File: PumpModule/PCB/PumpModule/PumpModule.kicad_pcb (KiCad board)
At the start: 2 copper layers, 8 parts, among them J5 Conn_01x04, J6 Conn_01x04, J7 Conn_01x03

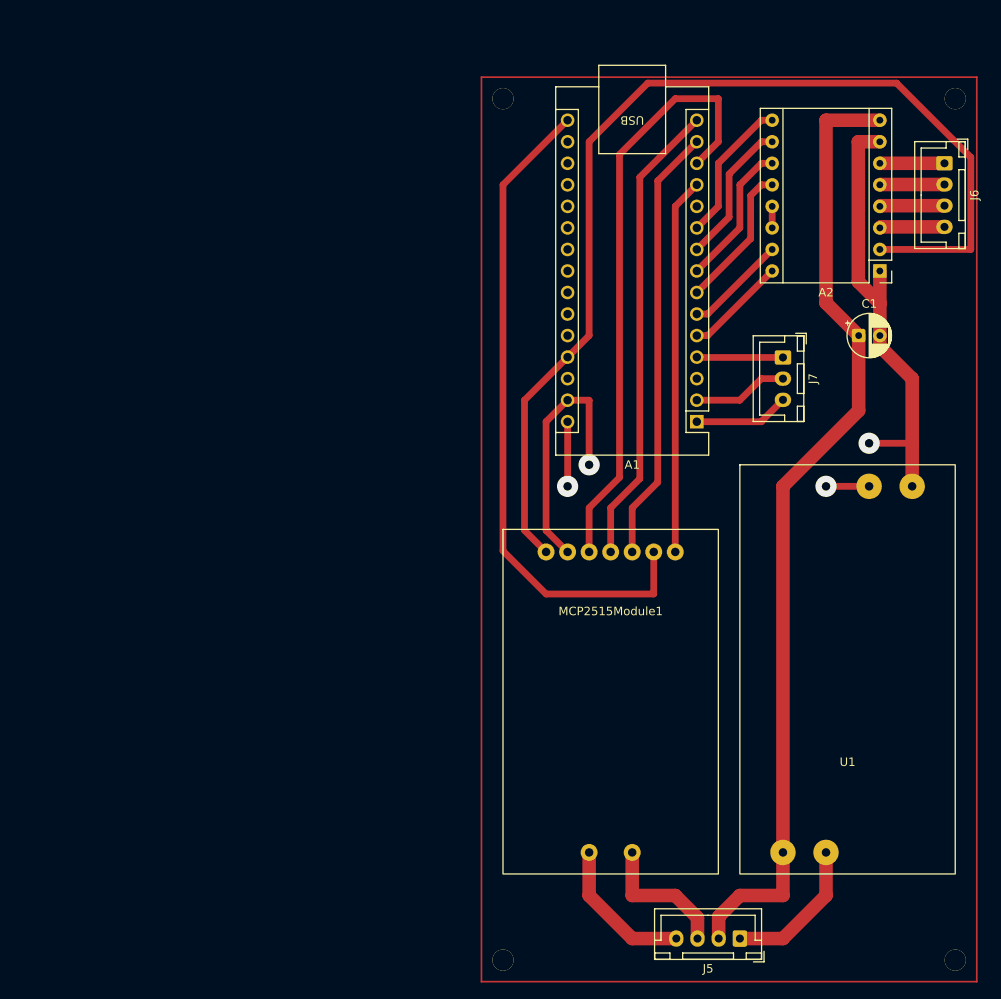
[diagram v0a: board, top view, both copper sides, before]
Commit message: [PCB] Made Pump v1.0 PCB
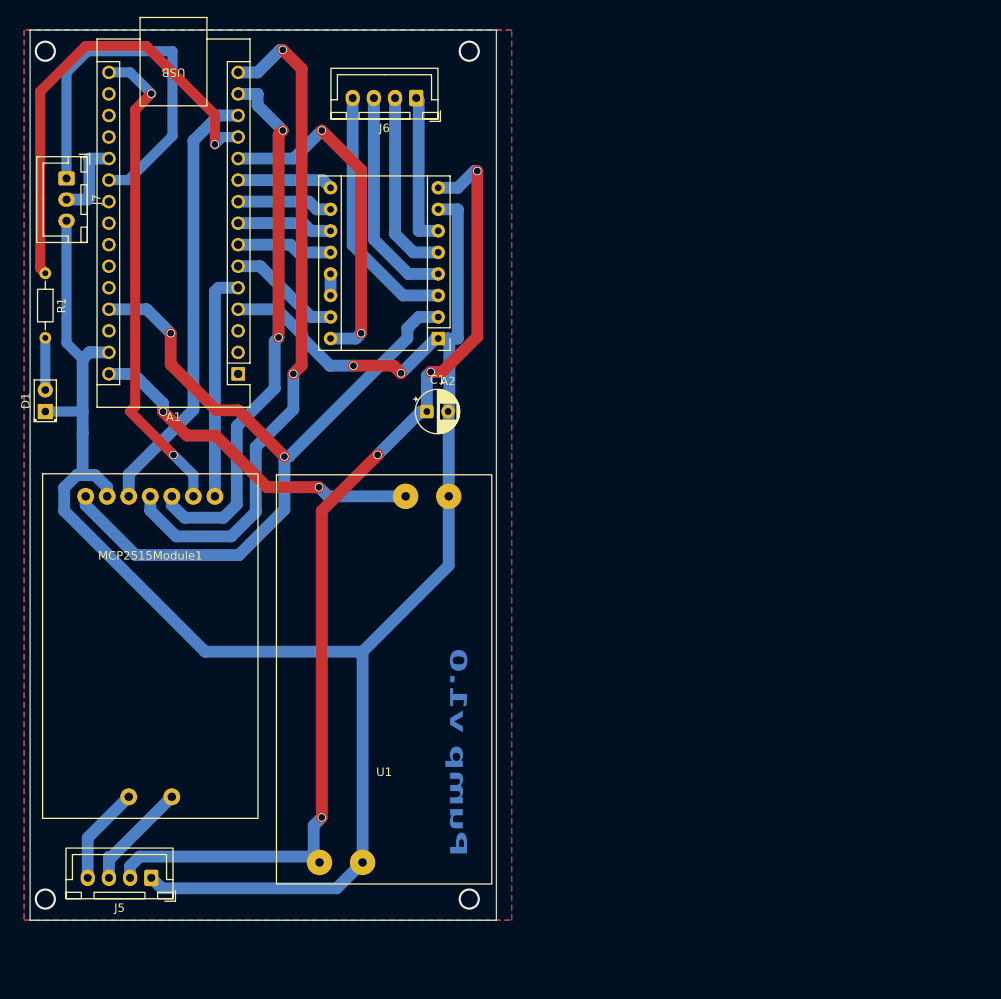
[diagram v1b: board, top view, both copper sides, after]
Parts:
- added D1: LED, LED_THT:LED_D2.0mm_W4.8mm_H2.5mm_FlatTop, F.Cu at (40.0, 75.0)
- added R1: R, Resistor_THT:R_Axial_DIN0204_L3.6mm_D1.6mm_P7.62mm_Horizontal, F.Cu at (40.0, 58.7)
- moved J7 87.1 mm to (42.5, 47.5)
- moved J5 69.8 mm to (52.5, 130.0)
- moved J6 62.8 mm to (83.8, 38.0), turned to 180 degrees
- moved MCP2515Module1 54.7 mm to (52.4, 92.5)
- moved U1 54.7 mm to (80.0, 118.0)
- moved A1 54.4 mm to (62.7, 70.6)
- moved A2 52.7 mm to (86.3, 66.4)
- moved C1 51.7 mm to (85.0, 75.0)
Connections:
- A1 pad 1: Net-(A1-D1/TX) -> unconnected-(A1-D1/TX-Pad1)
- A1 pad 11: unconnected-(A1-D8-Pad11) -> Net-(A1-D8)
- A1 pad 2: Net-(A1-D0/RX) -> unconnected-(A1-D0/RX-Pad2)
- A1 pad 20: unconnected-(A1-A1-Pad20) -> Net-(A1-A1)
- A1 pad 21: unconnected-(A1-A2-Pad21) -> Net-(A1-A2)
- A2 pad 16: Net-(A1-D2) -> Net-(A1-D8)
- J7 pad 1: GND -> Net-(A1-A2)
- J7 pad 2: Net-(A1-D0/RX) -> Net-(A1-A1)
- J7 pad 3: Net-(A1-D1/TX) -> GND
- MCP2515Module1 pad 7: Net-(A1-D9) -> Net-(A1-D2)
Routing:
- net GND: track 112.4 -> 232.1 mm
- net Net-(A1-A2): track 0.00 -> 45.7 mm
- net Net-(A1-D8): track 0.00 -> 40.9 mm, vias 0 -> 2
- net +5V: track 125.7 -> 91.1 mm, vias 0 -> 2
- net Net-(A1-VIN): track 12.7 -> 41.5 mm
- net Net-(A1-D12): track 55.1 -> 80.6 mm, vias 0 -> 2
- net Net-(A2-1B): track 7.67 -> 29.9 mm
- net Net-(A1-D13): track 78.8 -> 57.7 mm, vias 0 -> 2
- net Net-(A1-D10): track 71.4 -> 51.6 mm
- net Net-(A2-1A): track 7.65 -> 25.9 mm
- net Net-(A1-D2): track 12.0 -> 27.1 mm
- net Net-(A2-2A): track 7.64 -> 22.0 mm
- net Net-(A1-D11): track 51.5 -> 64.1 mm, vias 0 -> 2
- net Net-(A1-D1/TX): track 11.3 -> 0.00 mm
- net Net-(A1-D0/RX): track 11.2 -> 0.00 mm
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- added copper zone on B.Cu, net GND
- added copper zone on F.Cu, net GND
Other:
- board outline added: 55 x 105 mm
- board text added: "Pump v1.0"

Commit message: [PCB][PumpModule] Fixed input power pinout. Changed indication pin and add status LED to A0 pin
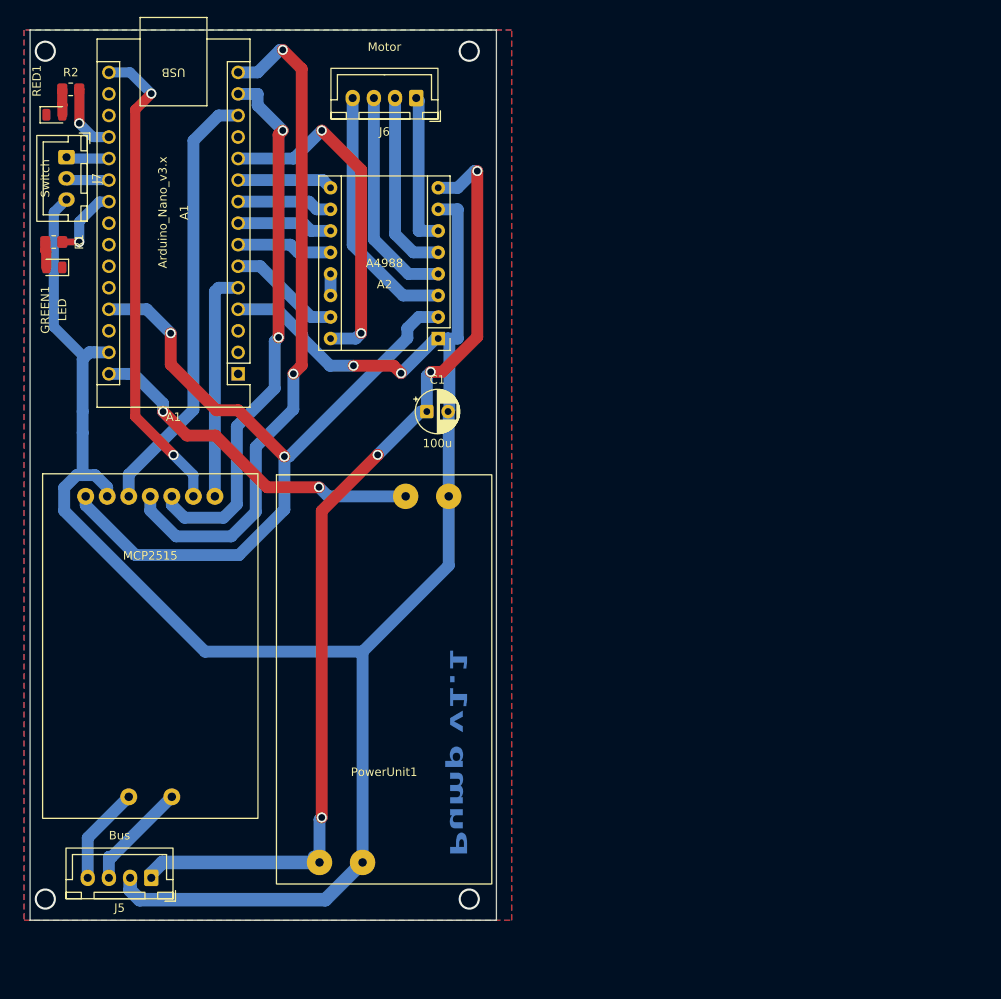
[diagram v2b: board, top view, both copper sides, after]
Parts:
- added R2: R, Resistor_SMD:R_0805_2012Metric_Pad1.20x1.40mm_HandSolder, F.Cu at (43.0, 37.0)
- added RED1: LED, LED_SMD:LED_0805_2012Metric, F.Cu at (41.1, 40.0)
- A2: value Pololu_Breakout_A4988 -> A4988
- GREEN1: renamed from D1; footprint LED_THT:LED_D2.0mm_W4.8mm_H2.5mm_FlatTop -> LED_SMD:LED_0805_2012Metric
- J5: value Conn_01x04 -> Bus
- J6: value Conn_01x04 -> Motor
- J7: value Conn_01x03 -> Switch
- R1: footprint Resistor_THT:R_Axial_DIN0204_L3.6mm_D1.6mm_P7.62mm_Horizontal -> Resistor_SMD:R_0805_2012Metric_Pad1.20x1.40mm_HandSolder
- moved GREEN1 17.0 mm to (41.1, 58.0), turned to 180 degrees
- moved R1 3.82 mm to (41.0, 55.0), turned to 180 degrees
- moved J7 2.50 mm to (42.5, 45.0)
- renumbered MCP2515Module1 to MCP2515, U1 to PowerUnit1
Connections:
- A1 pad 12: Net-(A1-D9) -> unconnected-(A1-D9-Pad12)
- A1 pad 19: unconnected-(A1-A0-Pad19) -> Net-(A1-A0)
- A1 pad 22: unconnected-(A1-A3-Pad22) -> Net-(A1-A3)
- J5 pad 1: GND -> +12V
- J5 pad 2: +12V -> GND
- J7 pad 1: Net-(A1-A2) -> Net-(A1-A1)
- J7 pad 2: Net-(A1-A1) -> Net-(A1-A2)
- R1 pad 1: Net-(A1-D9) -> Net-(A1-A3)
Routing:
- net Net-(A1-D9): track 54.4 -> 0.00 mm, vias 1 -> 0
- net Net-(A1-A2): track 45.7 -> 5.08 mm
- net Net-(A1-A3): track 0.00 -> 8.87 mm, vias 0 -> 1
- net Net-(A1-A0): track 0.00 -> 8.18 mm, vias 0 -> 1
- net Net-(A1-A1): track 9.71 -> 5.07 mm
- net GND: track 232.1 -> 235.9 mm
- net Net-(RED1-A): track 0.00 -> 3.01 mm
- net Net-(GREEN1-A): track 6.15 -> 3.22 mm
- net +12V: track 120.0 -> 117.7 mm
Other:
- board text added: "Pump v1.1"
- board text removed: "Pump v1.0"
